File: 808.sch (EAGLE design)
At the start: 56 parts, among them IC1 TL072D, T1 BC846, T2 BC846, T3 BC846, T5 BC846, T6 BC846

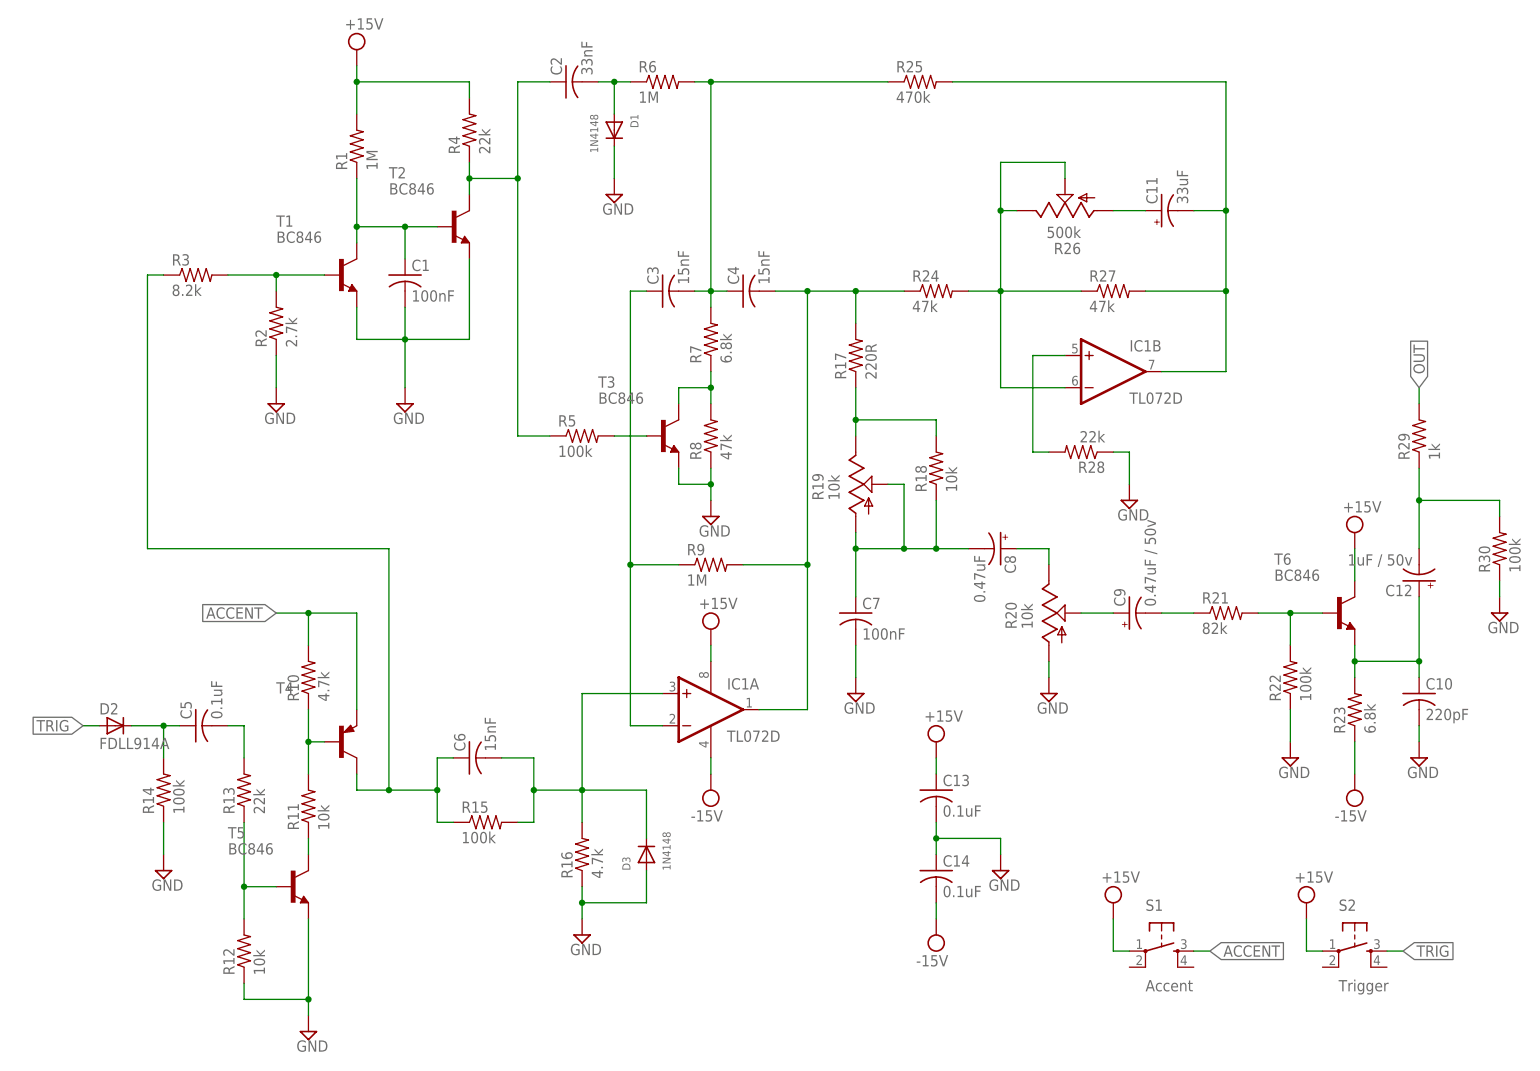
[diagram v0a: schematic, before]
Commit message: updating bom and pots
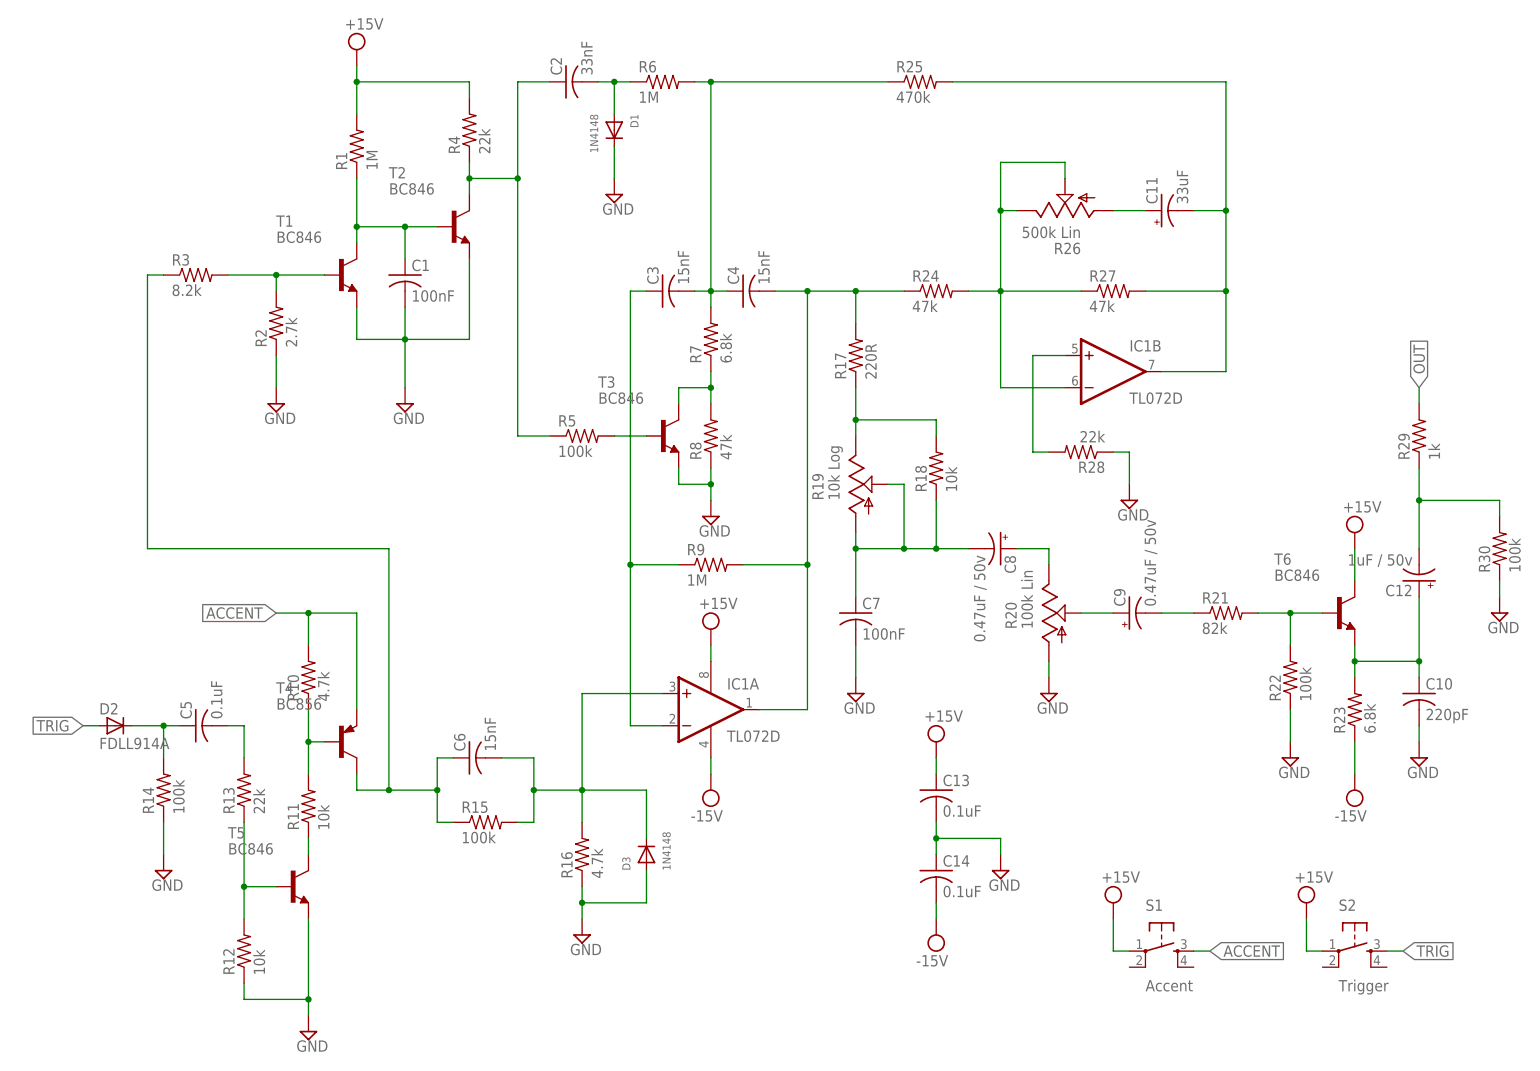
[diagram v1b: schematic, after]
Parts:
- C1, C13, C14, C5, C7: PARTNO (none) -> C0805C104K5RACTU
- C10: PARTNO (none) -> CC0805KRX7R9BB221
- C11: PARTNO (none) -> EEE-1AA330WAR
- C12: PARTNO (none) -> EEE-1HA010SR
- C2: PARTNO (none) -> CL21B333KBANNNC
- C3, C4, C6: PARTNO (none) -> CC0805KRX7R9BB153
- C8: value 0.47uF -> 0.47uF / 50v; PARTNO (none) -> EEE-1HAR47AR
- C9: PARTNO (none) -> EEE-1HAR47AR
- D1, D3: PARTNO (none) -> 1N4148WS
- D2: PARTNO (none) -> FDLL914A
- IC1: PARTNO (none) -> TL072SG-13
- R1, R6, R9: PARTNO (none) -> RC2012F105CS
- R10, R16: PARTNO (none) -> RMCF0805JT4K70
- R11, R12, R18: PARTNO (none) -> RC2012J103CS
- R13, R28, R4: PARTNO (none) -> RMCF0805JT22K0
- R14, R15, R22, R30, R5: PARTNO (none) -> RC2012J104CS
- R17: PARTNO (none) -> RMCF0805JT220R
- R19: value 10k -> 10k Log; device 808:POTTHUMB-3352 -> 808:POTPTV09-H; PARTNO (none) -> PTV09A-4020F-A103
- R2: PARTNO (none) -> RMCF0805JT2K70
- R20: value 10k -> 100k Lin; device 808:POTTHUMB-3352 -> 808:POTCTS296; PARTNO (none) -> 296UD104B1N
- R21: PARTNO (none) -> RMCF0805JT82K0
- R23, R7: PARTNO (none) -> MCR10ERTF6801
- R24, R27, R8: PARTNO (none) -> RMCF0805JT47K0
- R25: PARTNO (none) -> RMCF0805JT470K
- R26: value 500k -> 500k Lin; device 808:POTTHUMB-3352 -> 808:POTPTV09-H; PARTNO (none) -> 296UD504B1N
- R29: PARTNO (none) -> RC2012J102CS
- R3: PARTNO (none) -> RMCF0805JT8K20
- S1, S2: PARTNO (none) -> PTS525SM10SMTR LFS
- T1, T2, T3, T5, T6: PARTNO (none) -> BC846BMTF
- T4: value (none) -> BC856; PARTNO (none) -> BC856BMTF

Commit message: layout
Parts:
- added J1: HEADER, Livestream:HEADER
- added JP1: AUDIO-JACK-3P, Livestream:AUDIO-JACK-3P
- R19: value 10k Log -> Tone / 10k Log
- R20: value 100k Lin -> Level / 100k Lin
- R26: value 500k Lin -> Decay / 500k Lin
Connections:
- removed net VCC: C13.1, C14.2
- net +15V: now also C13.1, J1.2
- net -15V: now also C14.2, J1.1
- net GND: now also JP1.SLEEVE
- net OUT: now also JP1.LEFT, JP1.RIGHT
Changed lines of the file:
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@@
 </variantdefs>
 <classes>
-<class number="0" name="default" width="0" drill="0">
+<class number="0" name="default" width="0.1524" drill="0.3302">
+<clearance class="0" value="0.1524"/>
 </class>
 </classes>
@@
 </part>
 <part name="SUPPLY9" library="supply2" deviceset="GND" device=""/>
-<part name="R19" library="808" deviceset="POT" device="PTV09-H" value="10k Log">
+<part name="R19" library="808" deviceset="POT" device="PTV09-H" value="Tone / 10k Log">
 <attribute name="PARTNO" value="PTV09A-4020F-A103"/>
 </part>
@@
 <attribute name="PARTNO" value="EEE-1HAR47AR"/>
 </part>
-<part name="R20" library="808" deviceset="POT" device="CTS296" value="100k Lin">
+<part name="R20" library="808" deviceset="POT" device="CTS296" value="Level / 100k Lin">
 <attribute name="PARTNO" value="296UD104B1N"/>
 </part>
@@
 <attribute name="PARTNO" value="RMCF0805JT470K"/>
 </part>
-<part name="R26" library="808" deviceset="POT" device="PTV09-H" value="500k Lin">
+<part name="R26" library="808" deviceset="POT" device="PTV09-H" value="Decay / 500k Lin">
 <attribute name="PARTNO" value="296UD504B1N"/>
 </part>
@@
 <part name="SUPPLY22" library="supply2" deviceset="VCC" device="" value="+15V"/>
 <part name="SUPPLY23" library="supply2" deviceset="VCC" device="" value="+15V"/>
+<part name="JP1" library="Livestream" deviceset="AUDIO-JACK-3P" device=""/>
+<part name="SUPPLY24" library="supply2" deviceset="GND" device=""/>
+<part name="J1" library="Livestream" deviceset="HEADER" device=""/>
 </parts>
 <sheets>
@@
 <instance part="SUPPLY22" gate="G$1" x="53.34" y="17.78"/>
 <instance part="SUPPLY23" gate="G$1" x="83.82" y="17.78"/>
+<instance part="JP1" gate="G$1" x="111.76" y="134.62" rot="R180"/>
+<instance part="SUPPLY24" gate="GND" x="104.14" y="124.46"/>
+<instance part="J1" gate="G$1" x="7.62" y="27.94"/>
 </instances>
 <busses>
@@
 <wire x1="25.4" y1="25.4" x2="25.4" y2="27.94" width="0.1524" layer="91"/>
 <junction x="25.4" y="27.94"/>
+</segment>
+<segment>
+<pinref part="JP1" gate="G$1" pin="SLEEVE"/>
+<pinref part="SUPPLY24" gate="GND" pin="GND"/>
+<wire x1="106.68" y1="132.08" x2="104.14" y2="132.08" width="0.1524" layer="91"/>
+<wire x1="104.14" y1="132.08" x2="104.14" y2="127" width="0.1524" layer="91"/>
 </segment>
 </net>
@@
 <wire x1="-10.16" y1="40.64" x2="-10.16" y2="38.1" width="0.1524" layer="91"/>
 </segment>
+<segment>
+<pinref part="C14" gate="G$1" pin="2"/>
+<pinref part="SUPPLY20" gate="G$1" pin="VCC"/>
+<wire x1="25.4" y1="17.78" x2="25.4" y2="15.24" width="0.1524" layer="91"/>
+<pinref part="J1" gate="G$1" pin="1"/>
+<wire x1="15.24" y1="27.94" x2="17.78" y2="27.94" width="0.1524" layer="91"/>
+<wire x1="17.78" y1="27.94" x2="17.78" y2="17.78" width="0.1524" layer="91"/>
+<wire x1="17.78" y1="17.78" x2="25.4" y2="17.78" width="0.1524" layer="91"/>
+<junction x="25.4" y="17.78"/>
+</segment>
 </net>
 <net name="+15V" class="0">
@@
 <wire x1="83.82" y1="10.16" x2="83.82" y2="15.24" width="0.1524" layer="91"/>
 <pinref part="SUPPLY23" gate="G$1" pin="VCC"/>
+</segment>
+<segment>
+<pinref part="SUPPLY19" gate="G$1" pin="VCC"/>
+<pinref part="C13" gate="G$1" pin="1"/>
+<wire x1="25.4" y1="40.64" x2="25.4" y2="38.1" width="0.1524" layer="91"/>
+<pinref part="J1" gate="G$1" pin="2"/>
+<wire x1="15.24" y1="30.48" x2="17.78" y2="30.48" width="0.1524" layer="91"/>
+<wire x1="17.78" y1="30.48" x2="17.78" y2="38.1" width="0.1524" layer="91"/>
+<wire x1="17.78" y1="38.1" x2="25.4" y2="38.1" width="0.1524" layer="91"/>
+<junction x="25.4" y="38.1"/>
 </segment>
 </net>
@@
 <label x="101.6" y="99.06" size="1.778" layer="95" rot="R90" xref="yes"/>
 </segment>
-</net>
-<net name="VCC" class="0">
-<segment>
-<pinref part="SUPPLY19" gate="G$1" pin="VCC"/>
-<pinref part="C13" gate="G$1" pin="1"/>
-<wire x1="25.4" y1="40.64" x2="25.4" y2="38.1" width="0.1524" layer="91"/>
-</segment>
-<segment>
-<pinref part="C14" gate="G$1" pin="2"/>
-<pinref part="SUPPLY20" gate="G$1" pin="VCC"/>
-<wire x1="25.4" y1="17.78" x2="25.4" y2="15.24" width="0.1524" layer="91"/>
-</segment>
-</net>
+<segment>
+<pinref part="JP1" gate="G$1" pin="LEFT"/>
+<wire x1="106.68" y1="137.16" x2="104.14" y2="137.16" width="0.1524" layer="91"/>
+<pinref part="JP1" gate="G$1" pin="RIGHT"/>
+<wire x1="106.68" y1="134.62" x2="104.14" y2="134.62" width="0.1524" layer="91"/>
+<wire x1="104.14" y1="134.62" x2="104.14" y2="137.16" width="0.1524" layer="91"/>
+<wire x1="104.14" y1="137.16" x2="99.06" y2="137.16" width="0.1524" layer="91"/>
+<label x="99.06" y="137.16" size="1.778" layer="95" rot="R180" xref="yes"/>
+<junction x="104.14" y="137.16"/>
+</segment>
+</net>

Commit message: v0.1
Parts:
- JP1: PARTNO (none) -> SJ-3523-SMT-TR
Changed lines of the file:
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@@
 <part name="SUPPLY22" library="supply2" deviceset="VCC" device="" value="+15V"/>
 <part name="SUPPLY23" library="supply2" deviceset="VCC" device="" value="+15V"/>
-<part name="JP1" library="Livestream" deviceset="AUDIO-JACK-3P" device=""/>
+<part name="JP1" library="Livestream" deviceset="AUDIO-JACK-3P" device="">
+<attribute name="PARTNO" value="SJ-3523-SMT-TR"/>
+</part>
 <part name="SUPPLY24" library="supply2" deviceset="GND" device=""/>
 <part name="J1" library="Livestream" deviceset="HEADER" device=""/>
@@
 <instance part="SUPPLY22" gate="G$1" x="53.34" y="17.78"/>
 <instance part="SUPPLY23" gate="G$1" x="83.82" y="17.78"/>
-<instance part="JP1" gate="G$1" x="111.76" y="134.62" rot="R180"/>
+<instance part="JP1" gate="G$1" x="111.76" y="134.62" rot="R180">
+<attribute name="PARTNO" x="111.76" y="134.62" size="1.778" layer="96" display="off"/>
+</instance>
 <instance part="SUPPLY24" gate="GND" x="104.14" y="124.46"/>
 <instance part="J1" gate="G$1" x="7.62" y="27.94"/>
